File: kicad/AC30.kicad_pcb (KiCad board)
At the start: 2 copper layers, 173 x 126.5 mm, 122 parts, among them IC1 4013, IC10 555, IC11 4001, IC12 1489, IC13 4070, IC14 4053, IC15 1488, IC2 4001, IC3 4070, IC4 4558, IC5 4013, IC6 4053, IC7 4049, IC8 4013, IC9 4023, J1 SWITCHES, J12 Power input, J13 MOTOR, J14 MIC, J15 EAR, J2 LEDS, J3 Computer interface (COMP), J4 Control interface, J5 Terminal interface (TERM), Q1 2N5210, Q10 2N5087, Q11 2N5087, Q2 2N5210, Q3 2N5087, Q4 2N5210, Q5 2N5210, Q6 2N5210, Q7 2N5210, Q8 2N5210, Q9 2N5087

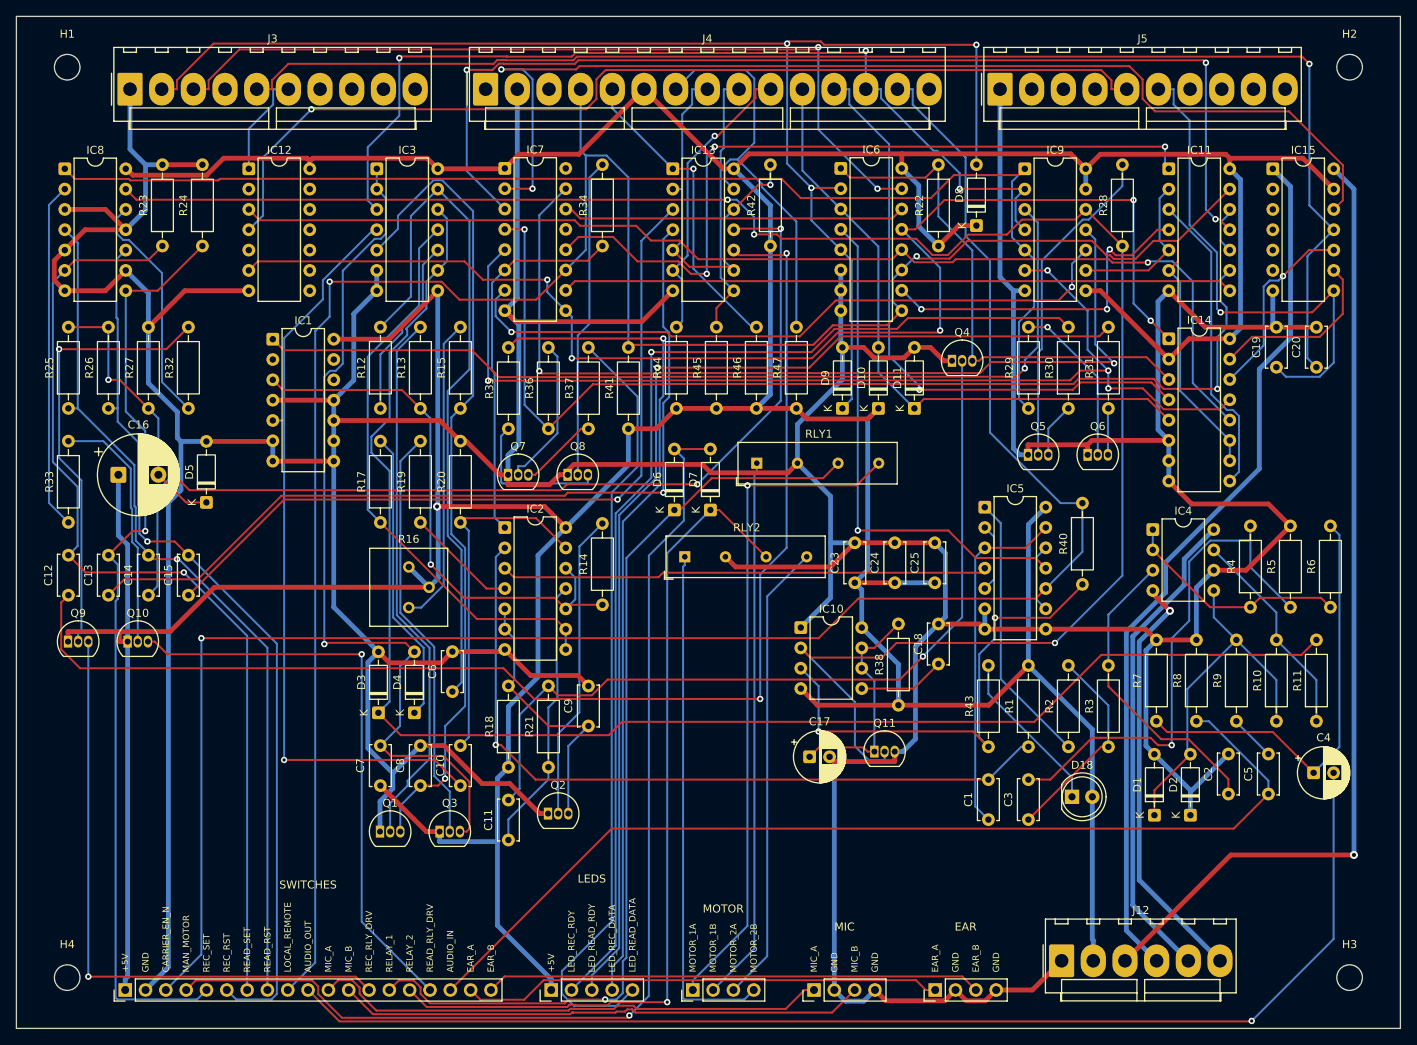
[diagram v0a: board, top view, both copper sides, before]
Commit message: Make the through-hole build route completely
The seed-30 placement boxed in Q8's collector, so R35-Q8 could not be
routed from scratch. Fixes:
- pcb.py: placement seed from AC30_SEED; build.sh tries seeds in turn
  (AC30_SEEDS; 31 32 34 through-hole, 30 31 32 SMT) until routing is clean
- route.py: finishing passes protect existing wiring except within
  ROUTE_FREE_RADIUS (5, 10, 20 mm) of the unrouted ends taken from DRC;
  a pass is kept when it reduces the unrouted count
- build.sh: early stop compares route summaries (track IDs are random);
  KiCad debug noise filtered
Through-hole board rebuilt with seed 31: 173.0 x 126.5 mm, routed on the
first attempt, ERC/DRC/parity clean. SMT board unchanged.

Co-Authored-By: Claude Opus 5.5 <noreply@anthropic.com>
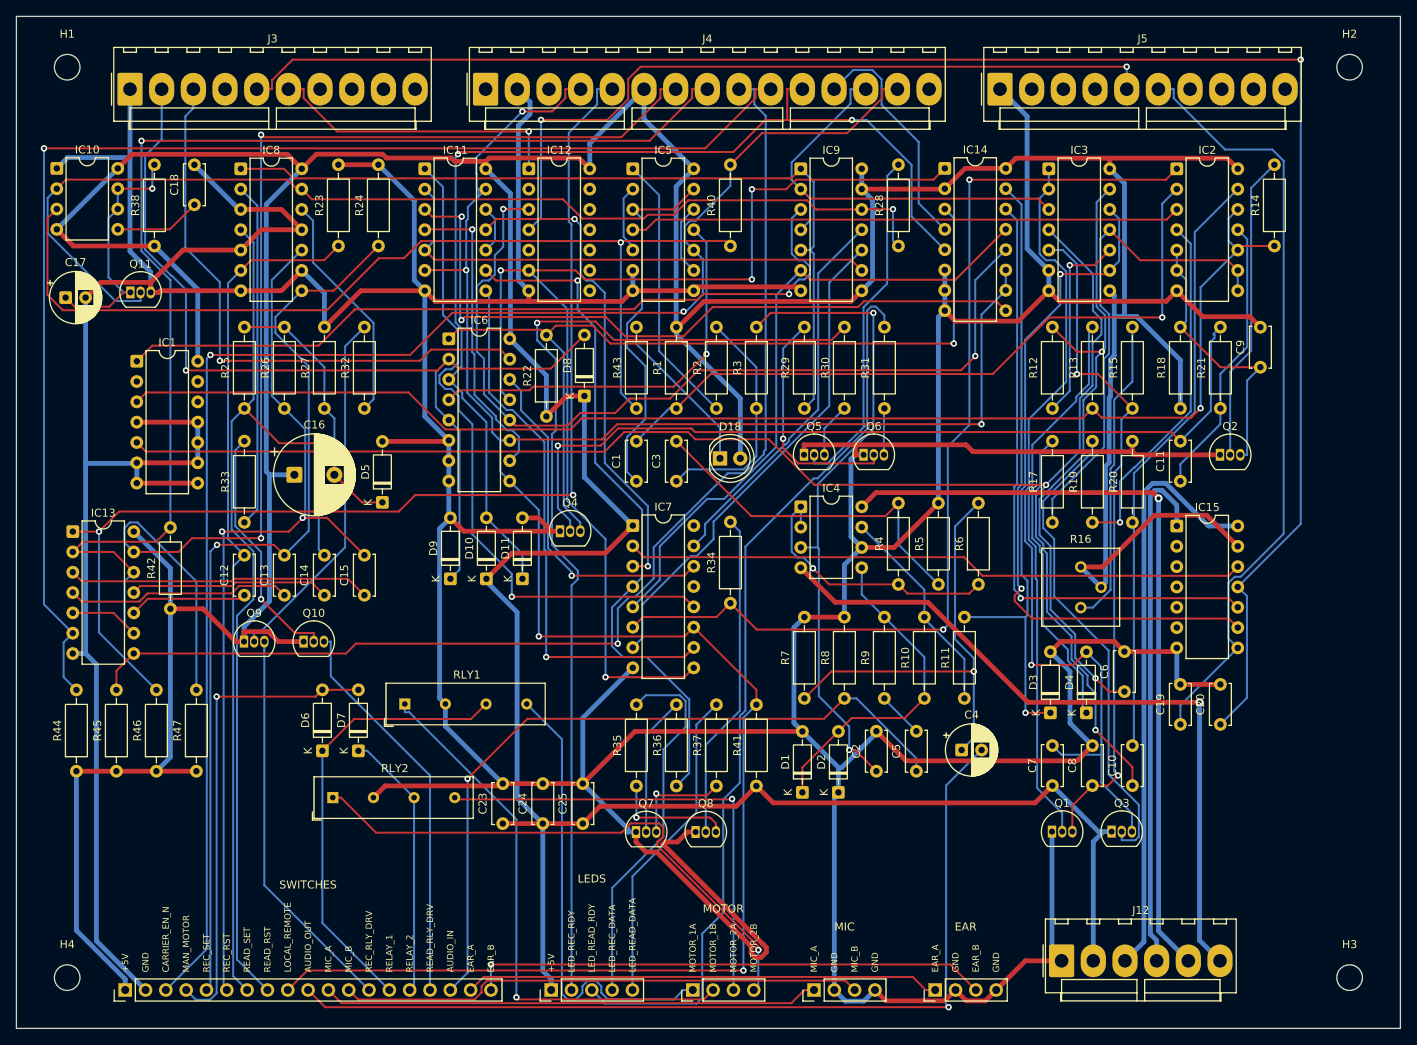
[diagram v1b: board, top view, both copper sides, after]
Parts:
- moved IC10 109.3 mm to (35.0, 48.5)
- moved C18 109.3 mm to (52.2, 53.0)
- moved Q11 109.3 mm to (44.2, 64.0)
- moved C17 109.3 mm to (36.1, 64.7)
- moved R38 109.3 mm to (47.2, 58.2)
- moved IC2 95.2 mm to (175.1, 48.5)
- moved C9 95.2 mm to (185.5, 73.3)
- moved C11 95.2 mm to (175.5, 87.6)
- moved Q2 95.2 mm to (180.4, 84.3)
- moved R14 95.2 mm to (187.2, 58.2)
- moved R18 95.2 mm to (175.5, 78.5)
- moved R21 95.2 mm to (180.5, 78.5)
- moved IC11 93.0 mm to (81.0, 48.5)
- moved IC13 87.6 mm to (37.0, 93.9)
- moved R42 87.6 mm to (49.2, 103.5)
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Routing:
- net /START_READ_P: track 161.1 -> 14.7 mm, vias 2 -> 0
- net /START_RECORD: track 36.9 -> 164.9 mm
- net /START_READ: track 33.4 -> 147.6 mm, vias 0 -> 1
- net /CTRL_INVERT: track 49.8 -> 163.3 mm
- net /Mod/Demod & power input/DEM_LIM: track 192.3 -> 83.0 mm, vias 0 -> 2
- net /REC_EN: track 240.3 -> 135.6 mm, vias 3 -> 1
- net /STOP_RECORD: track 39.0 -> 141.5 mm, vias 1 -> 2
- net /Mod/Demod & power input/DEM_BIT: track 96.1 -> 198.5 mm, vias 1 -> 2
- net /STOP_READ_P: track 125.2 -> 25.0 mm, vias 3 -> 0
- net /Mod/Demod & power input/DEM_PULSE: track 70.0 -> 169.9 mm
- net /STOP_READ: track 51.6 -> 151.5 mm, vias 0 -> 2
- net /START_REC_P: track 108.6 -> 28.2 mm, vias 1 -> 0
- net DATA_IN: track 47.0 -> 125.5 mm, vias 0 -> 2
- net /MAN_MOTOR: track 137.1 -> 59.8 mm
- net /CPU_RX_N: track 134.8 -> 61.2 mm, vias 3 -> 2
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
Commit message: Add a GND copper fill to both boards
tools/zones.py adds a GND zone on F.Cu and B.Cu over the whole outline
(0.3 mm clearance, 0.25 mm min width, 0.5/0.5 mm thermal reliefs, islands
removed); build.sh fills it with kicad-cli after routing. GND pads whose
thermal relief is starved get a solid connection, refilling until none is
left (11 pads through-hole, 2 SMT). FILL=0 builds without it.
Both boards ERC/DRC (all severities)/parity clean; Gerbers regenerated;
settings docs and README updated.

Co-Authored-By: Claude Opus 5.5 <noreply@anthropic.com>
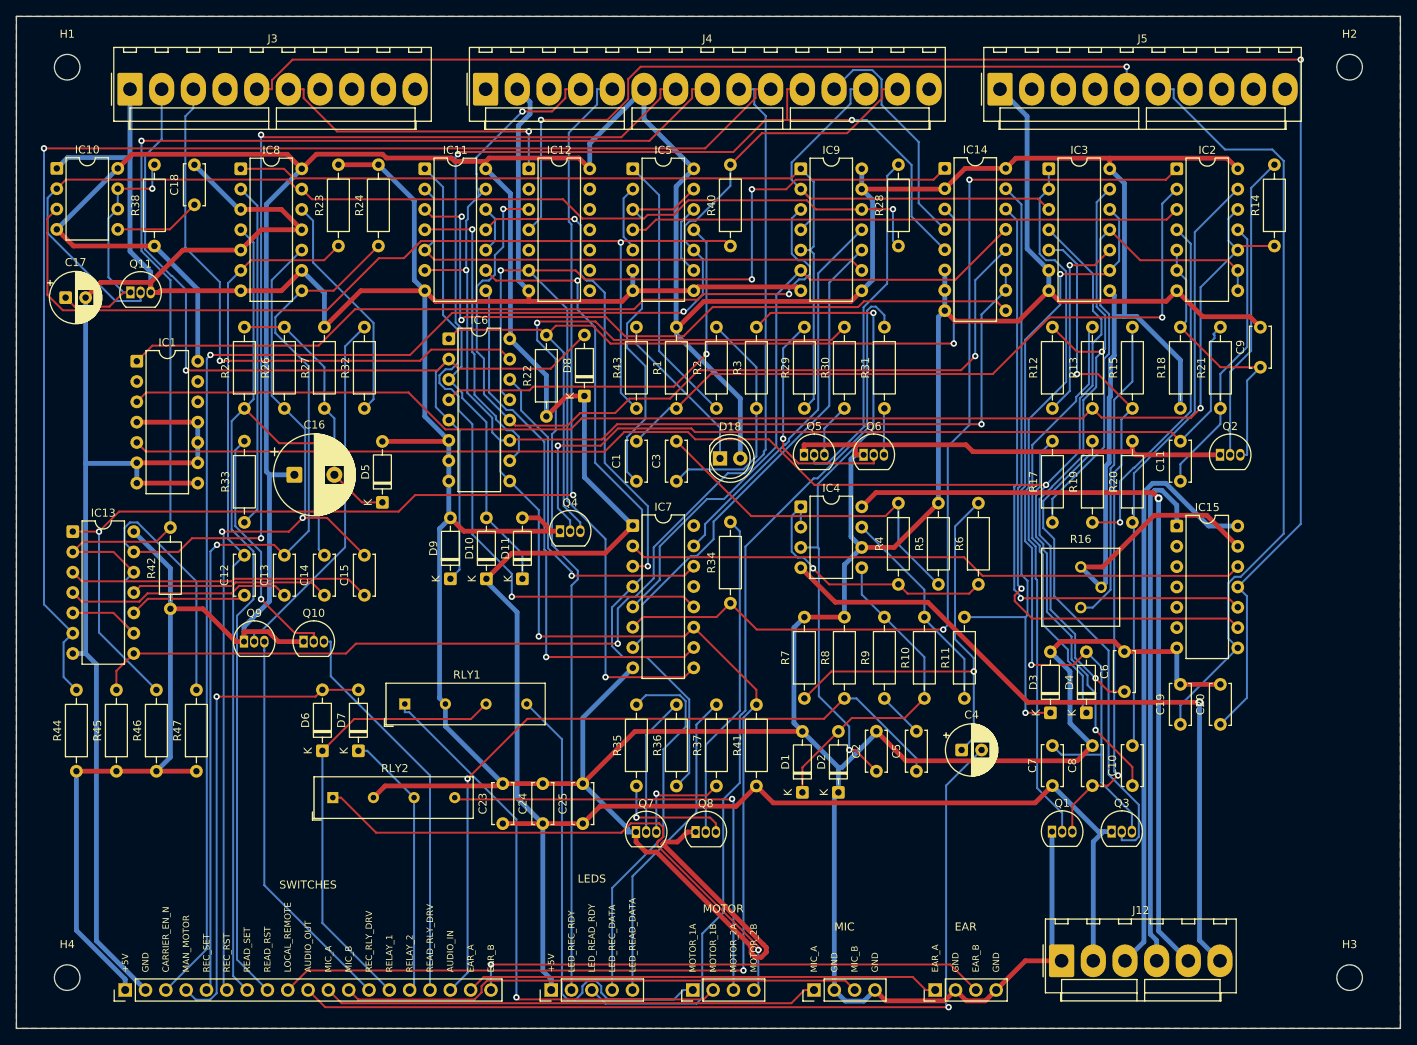
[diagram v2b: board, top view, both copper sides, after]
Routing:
- added copper zone on B.Cu, net GND
- added copper zone on F.Cu, net GND

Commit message: Motor and relay nets in the Power netclass
MOTOR_1A/1B/2A/2B and RELAY_1/2 now route as 0.6 mm tracks with 1.0/0.5 mm
vias (POWER_CLASS in pcb.py; placement unchanged). Both boards rebuilt:
routed on the first attempt, GND fill, ERC/DRC (all severities)/parity
clean. Gerbers regenerated; settings docs updated.

Co-Authored-By: Claude Opus 5.5 <noreply@anthropic.com>
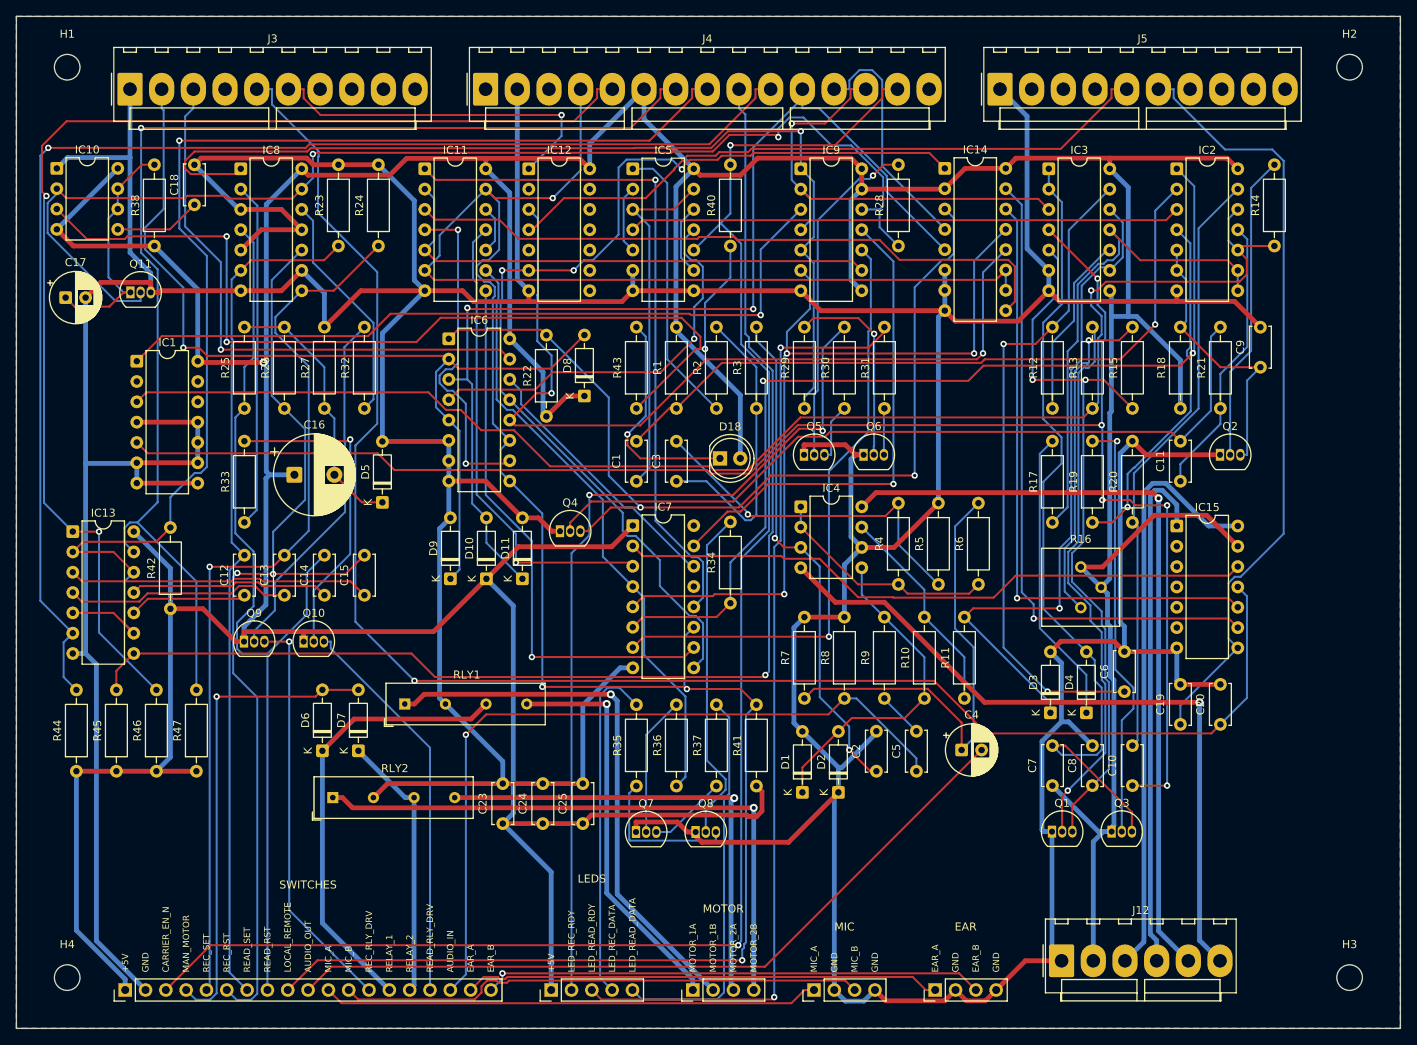
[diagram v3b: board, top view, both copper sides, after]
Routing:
- net GND: track 958.7 -> 903.0 mm
- net /TAPE_DATA_N: track 80.7 -> 102.4 mm, vias 0 -> 3
- net /TERM_DATA: track 151.3 -> 130.0 mm, vias 4 -> 3
- net /READ_EN: track 103.6 -> 124.1 mm, vias 0 -> 1
- net AUDIO_OUT: track 115.1 -> 96.6 mm, vias 1 -> 0
- net /Mod/Demod & power input/MOD_F2: track 81.1 -> 63.5 mm
- net /LED_REC_RDY: track 126.3 -> 109.6 mm, vias 1 -> 2
- net CARRIER_EN_N: track 191.8 -> 207.7 mm
- net /LOCAL_REMOTE: track 294.3 -> 309.9 mm, vias 5 -> 4
- net /REC_DATA_N: track 62.0 -> 76.0 mm, vias 0 -> 1
- net /START_READ: track 147.6 -> 161.1 mm
- net /DATA_SEL_N: track 48.3 -> 61.6 mm, vias 0 -> 1
- net +5V: track 759.1 -> 745.9 mm, vias 0 -> 1
- net /REC_EN: track 135.6 -> 148.2 mm, vias 1 -> 2
- net /CPU_RS232_IN: track 220.9 -> 208.5 mm
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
